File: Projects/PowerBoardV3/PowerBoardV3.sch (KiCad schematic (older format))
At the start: 0 parts

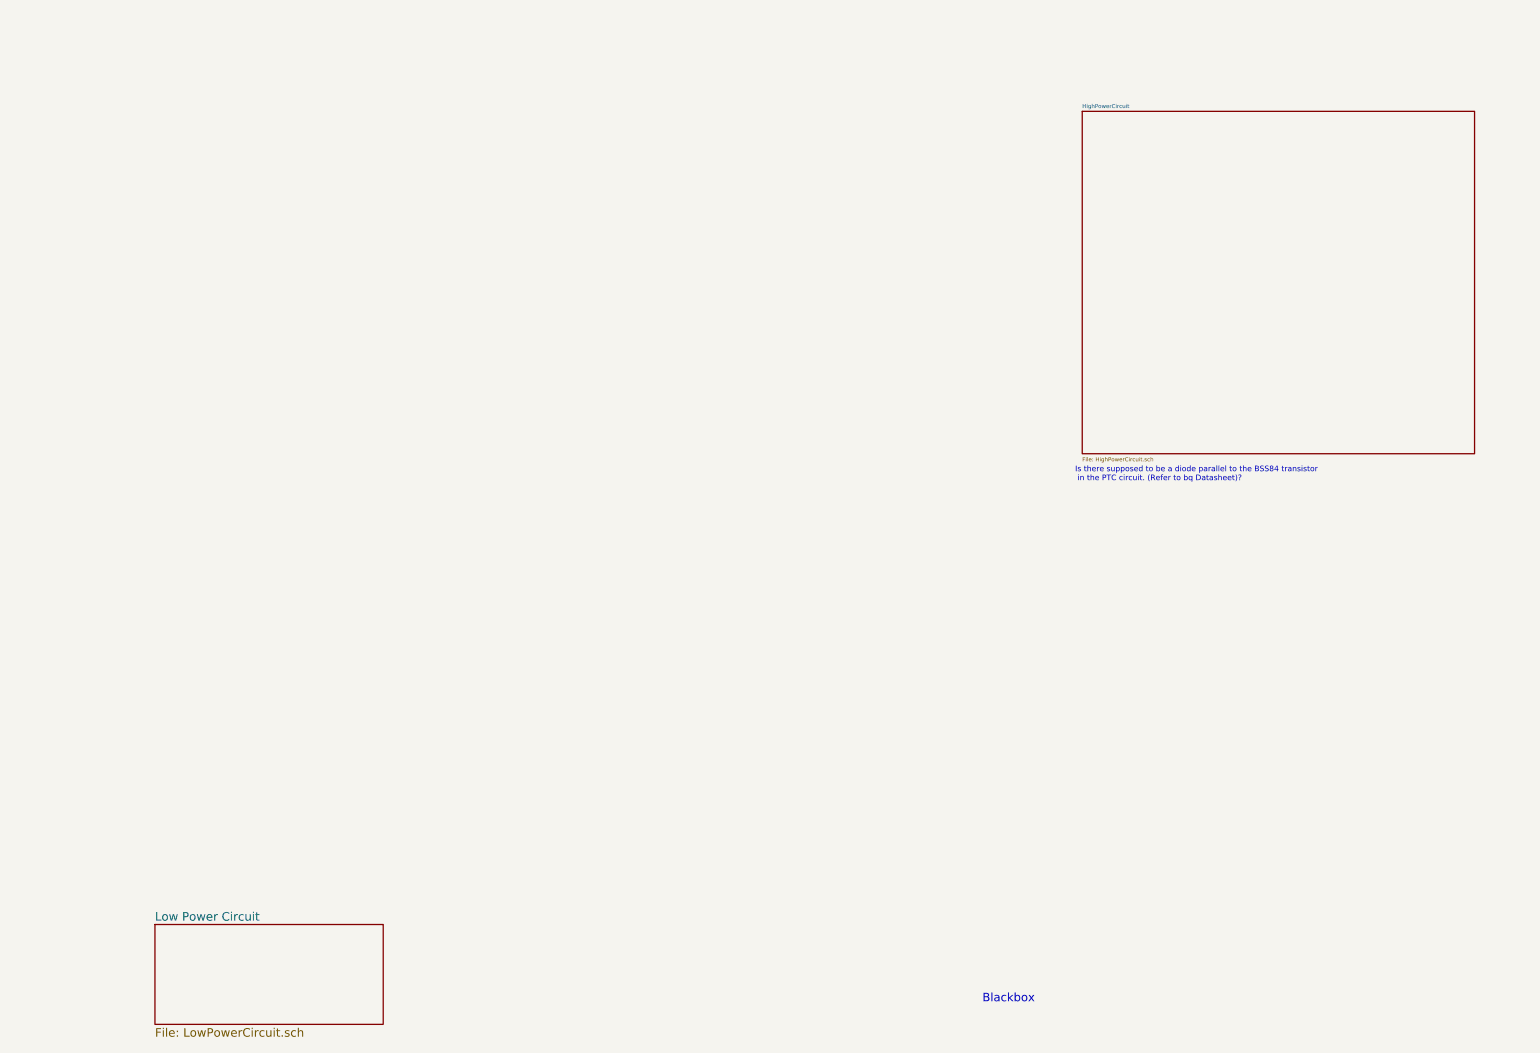
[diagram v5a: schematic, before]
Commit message: Created top level connections
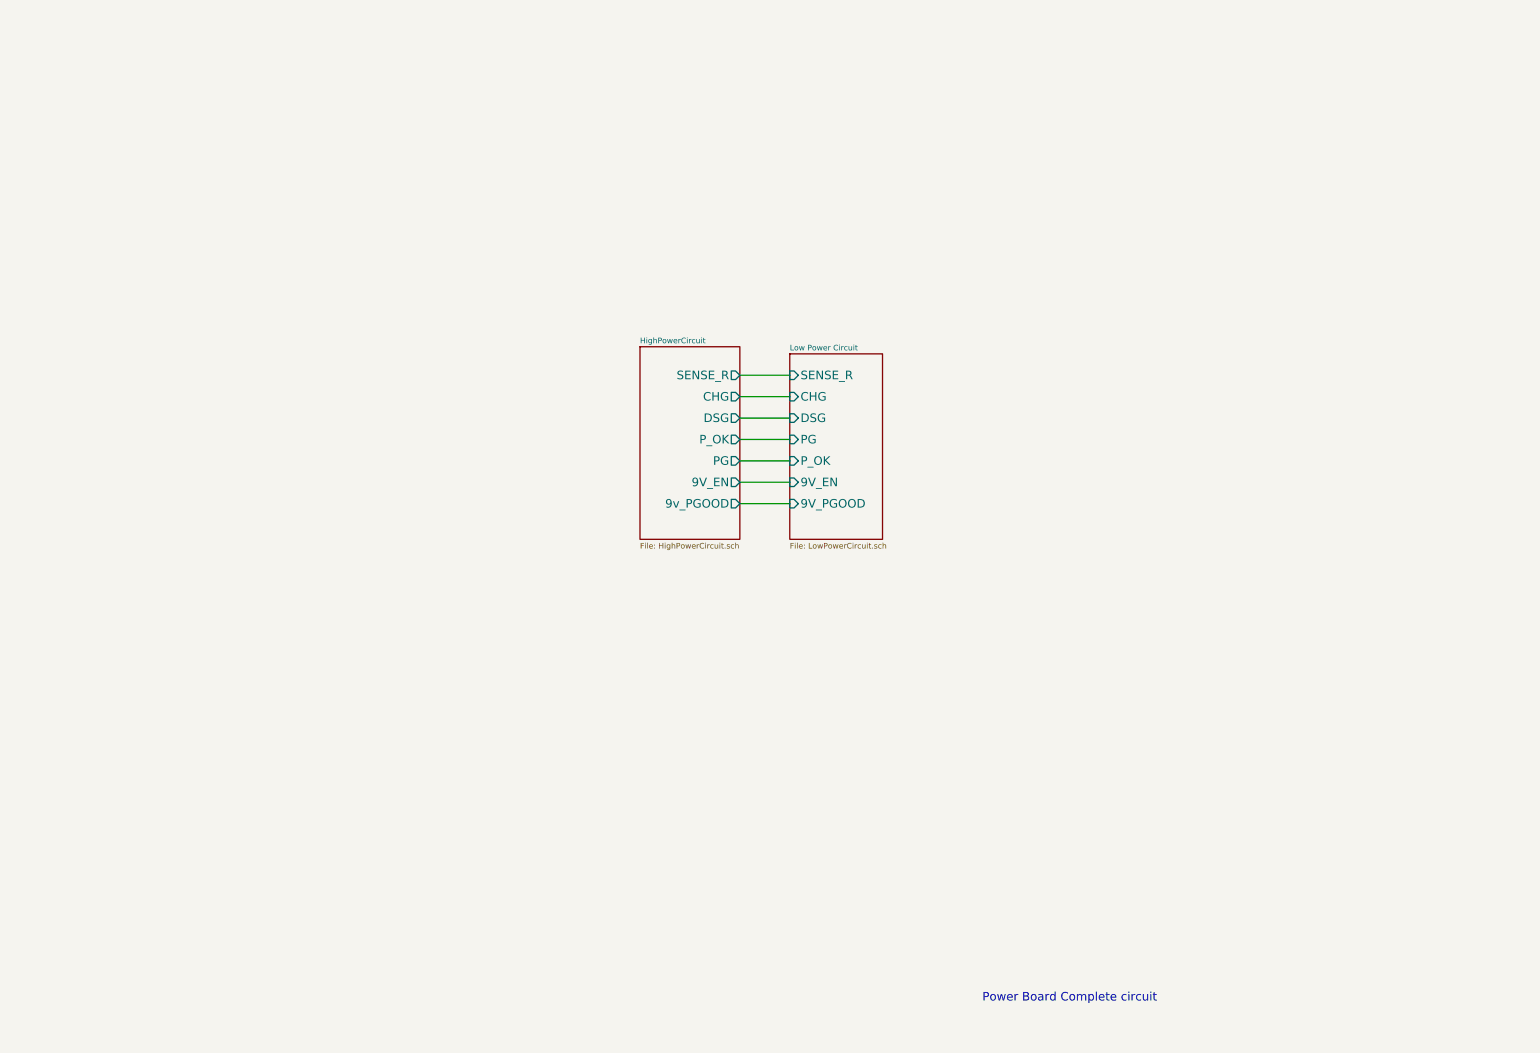
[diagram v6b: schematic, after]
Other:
- note added: "Power Board Complete circuit"
- note removed: "Blackbox\n\n"
- note removed: "Is there supposed to be a diode parallel to the BSS84 transistor\n in the PTC circuit. (Refer to bq Datasheet)?"
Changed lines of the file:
@@
 LIBS:valves
 LIBS:USST-parts
-LIBS:dk_Addressable-Specialty
-LIBS:dk_Alarms-Buzzers-and-Sirens
-LIBS:dk_Automotive-Relays
-LIBS:dk_Balun
-LIBS:dk_Barrel-Audio-Connectors
-LIBS:dk_Battery-Holders-Clips-Contacts
-LIBS:dk_Clock-Timing-Clock-Generators-PLLs-Frequency-Synthesizers
-LIBS:dk_Clock-Timing-Programmable-Timers-and-Oscillators
-LIBS:dk_Clock-Timing-Real-Time-Clocks
-LIBS:dk_Coaxial-Connectors-RF
-LIBS:dk_Current-Transducers
-LIBS:dk_Data-Acquisition-ADCs-DACs-Special-Purpose
-LIBS:dk_Data-Acquisition-Analog-to-Digital-Converters-ADC
-LIBS:dk_Data-Acquisition-Digital-Potentiometers
-LIBS:dk_Data-Acquisition-Digital-to-Analog-Converters-DAC
-LIBS:dk_Data-Acquisition-Touch-Screen-Controllers
-LIBS:dk_DC-DC-Converters
-LIBS:dk_Digital-Isolators
-LIBS:dk_Diodes-Bridge-Rectifiers
-LIBS:dk_Diodes-Rectifiers-Arrays
-LIBS:dk_Diodes-Rectifiers-Single
-LIBS:dk_Diodes-Zener-Single
-LIBS:dk_Display-Modules-LED-Character-and-Numeric
-LIBS:dk_D-Sub-Connectors
-LIBS:dk_Embedded-Microcontrollers
-LIBS:dk_Encoders
-LIBS:dk_Evaluation-Boards-Sensors
-LIBS:dk_Ferrite-Beads-and-Chips
-LIBS:dk_Fixed-Inductors
-LIBS:dk_Fuses
-LIBS:dk_Gas-Sensors
-LIBS:dk_Humidity-Moisture-Sensors
-LIBS:dk_Image-Sensors-Camera
-LIBS:dk_Infrared-UV-Visible-Emitters
-LIBS:dk_Inrush-Current-Limiters-ICL
-LIBS:dk_Interface-Analog-Switches-Multiplexers-Demultiplexers
-LIBS:dk_Interface-Analog-Switches-Special-Purpose
-LIBS:dk_Interface-Controllers
-LIBS:dk_Interface-Drivers-Receivers-Transceivers
-LIBS:dk_Interface-I-O-Expanders
-LIBS:dk_Interface-Modules
-LIBS:dk_Interface-Sensor-and-Detector-Interfaces
-LIBS:dk_Interface-Sensor-Capacitive-Touch
-LIBS:dk_Interface-Specialized
-LIBS:dk_LED-Indication-Discrete
-LIBS:dk_LEDs-Circuit-Board-Indicators-Arrays-Light-Bars-Bar-Graphs
-LIBS:dk_Linear-Amplifiers-Audio
-LIBS:dk_Linear-Amplifiers-Instrumentation-OP-Amps-Buffer-Amps
-LIBS:dk_Linear-Comparators
-LIBS:dk_Logic-Buffers-Drivers-Receivers-Transceivers
-LIBS:dk_Logic-Flip-Flops
-LIBS:dk_Logic-Gates-and-Inverters
-LIBS:dk_Logic-Multivibrators
-LIBS:dk_Logic-Shift-Registers
-LIBS:dk_Logic-Signal-Switches-Multiplexers-Decoders
-LIBS:dk_Logic-Translators-Level-Shifters
-LIBS:dk_Magnetic-Sensors-Compass-Magnetic-Field-Modules
-LIBS:dk_Magnetic-Sensors-Linear-Compass-ICs
-LIBS:dk_Magnetic-Sensors-Switches-Solid-State
-LIBS:dk_Memory
-LIBS:dk_Memory-Connectors-PC-Card-Sockets
-LIBS:dk_Microphones
-LIBS:dk_Modular-Connectors-Jacks
-LIBS:dk_Modular-Connectors-Jacks-With-Magnetics
-LIBS:dk_Motion-Sensors-Accelerometers
-LIBS:dk_Motion-Sensors-IMUs-Inertial-Measurement-Units
-LIBS:dk_Motion-Sensors-Tilt-Switches
-LIBS:dk_Navigation-Switches-Joystick
-LIBS:dk_Optical-Sensors-Ambient-Light-IR-UV-Sensors
-LIBS:dk_Optical-Sensors-Photo-Detectors-Remote-Receiver
-LIBS:dk_Optical-Sensors-Photodiodes
-LIBS:dk_Optical-Sensors-Phototransistors
-LIBS:dk_Optical-Sensors-Reflective-Analog-Output
-LIBS:dk_Optoisolators-Logic-Output
-LIBS:dk_Optoisolators-Transistor-Photovoltaic-Output
-LIBS:dk_Optoisolators-Triac-SCR-Output
-LIBS:dk_Oscillators
-LIBS:dk_PMIC-AC-DC-Converters-Offline-Switchers
-LIBS:dk_PMIC-Battery-Chargers
-LIBS:dk_PMIC-Battery-Management
-LIBS:dk_PMIC-Current-Regulation-Management
-LIBS:dk_PMIC-Full-Half-Bridge-Drivers
-LIBS:dk_PMIC-Gate-Drivers
-LIBS:dk_PMIC-LED-Drivers
-LIBS:dk_PMIC-Motor-Drivers-Controllers
-LIBS:dk_PMIC-OR-Controllers-Ideal-Diodes
-LIBS:dk_PMIC-Power-Distribution-Switches-Load-Drivers
-LIBS:dk_PMIC-Power-Management-Specialized
-LIBS:dk_PMIC-RMS-to-DC-Converters
-LIBS:dk_PMIC-Supervisors
-LIBS:dk_PMIC-Thermal-Management
-LIBS:dk_PMIC-V-F-and-F-V-Converters
-LIBS:dk_PMIC-Voltage-Reference
-LIBS:dk_PMIC-Voltage-Regulators-DC-DC-Switching-Controllers
-LIBS:dk_PMIC-Voltage-Regulators-DC-DC-Switching-Regulators
-LIBS:dk_PMIC-Voltage-Regulators-Linear
-LIBS:dk_PMIC-Voltage-Regulators-Special-Purpose
-LIBS:dk_Power-Relays-Over-2-Amps
-LIBS:dk_Pressure-Sensors-Transducers
-LIBS:dk_Programmable-Oscillators
-LIBS:dk_Pushbutton-Switches
-LIBS:dk_Rectangular-Connectors-Headers-Male-Pins
-LIBS:dk_Reed-Relays
-LIBS:dk_Resistor-Networks-Arrays
-LIBS:dk_RF-Amplifiers
-LIBS:dk_RF-Antennas
-LIBS:dk_RF-Demodulators
-LIBS:dk_RF-Detectors
-LIBS:dk_RF-Evaluation-and-Development-Kits-Boards
-LIBS:dk_RFID-RF-Access-Monitoring-ICs
-LIBS:dk_RF-Receivers
-LIBS:dk_RF-Switches
-LIBS:dk_RF-Transceiver-ICs
-LIBS:dk_RF-Transceiver-Modules
-LIBS:dk_RF-Transmitters
-LIBS:dk_Rotary-Potentiometers-Rheostats
-LIBS:dk_Sensors-Transducers_Accessories
-LIBS:dk_Signal-Relays-Up-to-2-Amps
-LIBS:dk_Slide-Switches
-LIBS:dk_Solid-State-Relays
-LIBS:dk_Specialized-ICs
-LIBS:dk_Specialized-Sensors
-LIBS:dk_Surge-Suppression-ICs
-LIBS:dk_Tactile-Switches
-LIBS:dk_Temperature-Sensors-Analog-and-Digital-Output
-LIBS:dk_Thermal-Cutoffs-Thermal-Fuses
-LIBS:dk_Thyristors-DIACs-SIDACs
-LIBS:dk_Thyristors-SCRs
-LIBS:dk_Thyristors-TRIACs
-LIBS:dk_Toggle-Switches
-LIBS:dk_Transistors-Bipolar-BJT-Arrays
-LIBS:dk_Transistors-Bipolar-BJT-RF
-LIBS:dk_Transistors-Bipolar-BJT-Single
-LIBS:dk_Transistors-Bipolar-BJT-Single-Pre-Biased
-LIBS:dk_Transistors-FETs-MOSFETs-Arrays
-LIBS:dk_Transistors-FETs-MOSFETs-RF
-LIBS:dk_Transistors-FETs-MOSFETs-Single
-LIBS:dk_Transistors-JFETs
-LIBS:dk_Trimmer-Potentiometers
-LIBS:dk_TVS-Diodes
-LIBS:dk_TVS-Mixed-Technology
-LIBS:dk_USB-DVI-HDMI-Connectors
 LIBS:PowerBoardV3-cache
 EELAYER 25 0
@@
 Comment4 ""
 $EndDescr
-Text Notes 7350 7600 0    59   ~ 0
-Blackbox\n\n
 $Sheet
-S 8050 1250 2750 2400
+S 4950 2900 700  1350
 U 5AA250C9
-F0 "HighPowerCircuit" 28
-F1 "HighPowerCircuit.sch" 28
+F0 "HighPowerCircuit" 39
+F1 "HighPowerCircuit.sch" 39
+F2 "SENSE_R" O R 5650 3100 60
+F3 "CHG" O R 5650 3250 60
+F4 "DSG" O R 5650 3400 60
+F5 "P_OK" O R 5650 3550 60
+F6 "PG" O R 5650 3700 60
+F7 "9V_EN" O R 5650 3850 60
+F8 "9v_PGOOD" O R 5650 4000 60
 $EndSheet
 $Sheet
-S 1550 6950 1600 700
+S 6000 2950 650  1300
 U 5AA20151
-F0 "Low Power Circuit " 60
-F1 "LowPowerCircuit.sch" 60
+F0 "Low Power Circuit " 39
+F1 "LowPowerCircuit.sch" 39
+F2 "SENSE_R" I L 6000 3100 60
+F3 "CHG" I L 6000 3250 60
+F4 "DSG" I L 6000 3400 60
+F5 "PG" I L 6000 3550 60
+F6 "P_OK" I L 6000 3700 60
+F7 "9V_EN" I L 6000 3850 60
+F8 "9V_PGOOD" I L 6000 4000 60
 $EndSheet
-Text Notes 8000 3850 0    39   ~ 0
-Is there supposed to be a diode parallel to the BSS84 transistor\n in the PTC circuit. (Refer to bq Datasheet)?
+Wire Wire Line
+	5650 3100 6000 3100
+Wire Wire Line
+	5650 3250 6000 3250
+Wire Wire Line
+	5650 3400 6000 3400
+Wire Wire Line
+	5650 3550 6000 3550
+Wire Wire Line
+	5650 3700 6000 3700
+Wire Wire Line
+	5650 3850 6000 3850
+Wire Wire Line
+	5650 4000 6000 4000
+Text Notes 7350 7500 0    60   ~ 0
+Power Board Complete circuit
 $EndSCHEMATC

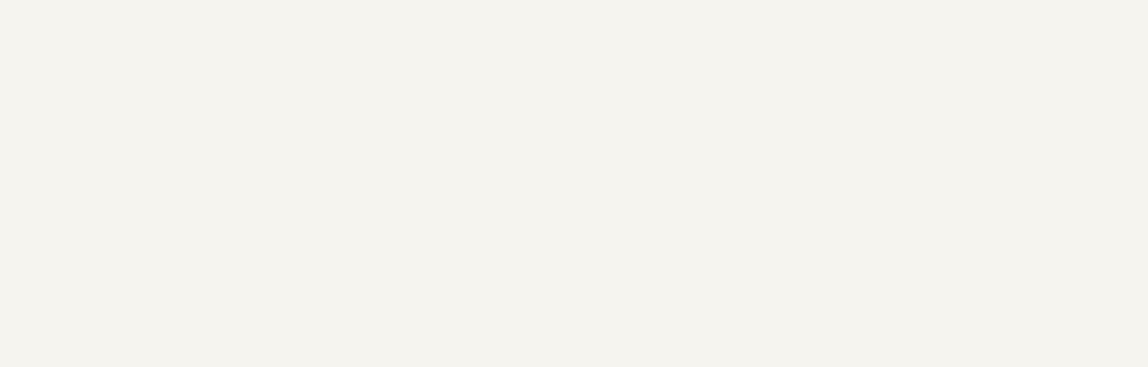
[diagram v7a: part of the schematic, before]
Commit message: Added more Footprint
Associated Resistors, Inductor and SAMD21 and placed their respective values and part numbers in the BOM
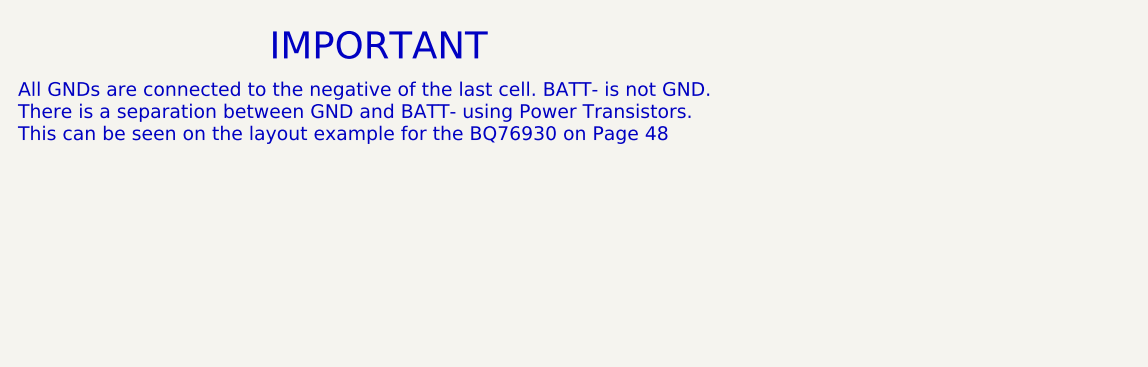
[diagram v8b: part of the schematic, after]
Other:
- note added: "All GNDs are connected to the negative of the last cell. BATT- is not GND. \nThere is a separation between GND and BATT- using Power Transistors. \nThis can be seen on the layout example for the BQ76930 on Page 48\n"
- note added: "IMPORTANT"
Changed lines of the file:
@@
 Text Notes 7350 7500 0    60   ~ 0
 Power Board Complete circuit
+Text Notes 2650 1100 0    60   ~ 0
+All GNDs are connected to the negative of the last cell. BATT- is not GND. \nThere is a separation between GND and BATT- using Power Transistors. \nThis can be seen on the layout example for the BQ76930 on Page 48\n
+Text Notes 3750 750  0    118  ~ 0
+IMPORTANT
 $EndSCHEMATC
